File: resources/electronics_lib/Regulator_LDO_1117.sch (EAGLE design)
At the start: 3 parts

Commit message: Simplified some schematic blocks.
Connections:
- net 1_2V,#,+,O/1_8V,#,+,O/2_5V,#,+,O/2_85V,#,+,O/3_3V,#,+,O/5V,#,+,O renamed 3_3V,#,+,O
- net V_SUPPLY,#,+,I/V_BATT,#,+,I/2_5V,#,+,I/2_85V,#,+,I/3V,#,+,I/3_3V,#,+,I/3_6V,#,+,I/3_7V,#,+,I/4_5V,#,+,I/4_8V,#,+,I/5V,#,+,I/6V,#,+,I/7_2V,#,+,I/7_4V,#,+,I/7_5V,#,+,I/8_4V,#,+,I/9V,#,+,I/9_6V,#,+,I/10_5V,#,+,I/11_1V,#,+,I/12V,#,+,I renamed 5V,#,+,I
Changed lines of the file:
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@@
 </segment>
 </net>
-<net name="1_2V,#,+,O/1_8V,#,+,O/2_5V,#,+,O/2_85V,#,+,O/3_3V,#,+,O/5V,#,+,O" class="0">
+<net name="3_3V,#,+,O" class="0">
 <segment>
 <pinref part="C_BYP_OUT_1" gate="G$1" pin="1"/>
@@
 </segment>
 </net>
-<net name="V_SUPPLY,#,+,I/V_BATT,#,+,I/2_5V,#,+,I/2_85V,#,+,I/3V,#,+,I/3_3V,#,+,I/3_6V,#,+,I/3_7V,#,+,I/4_5V,#,+,I/4_8V,#,+,I/5V,#,+,I/6V,#,+,I/7_2V,#,+,I/7_4V,#,+,I/7_5V,#,+,I/8_4V,#,+,I/9V,#,+,I/9_6V,#,+,I/10_5V,#,+,I/11_1V,#,+,I/12V,#,+,I" class="0">
+<net name="5V,#,+,I" class="0">
 <segment>
 <pinref part="C_BYP_IN_1" gate="G$1" pin="1"/>

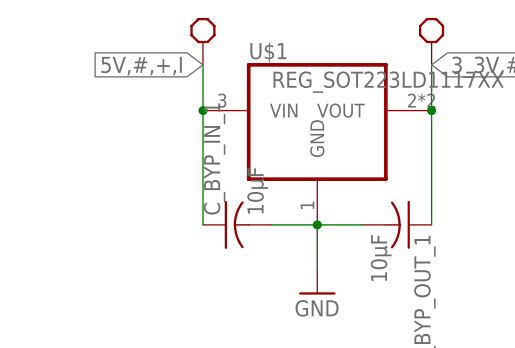
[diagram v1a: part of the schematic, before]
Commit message: Updated voltage setting in Regulator.
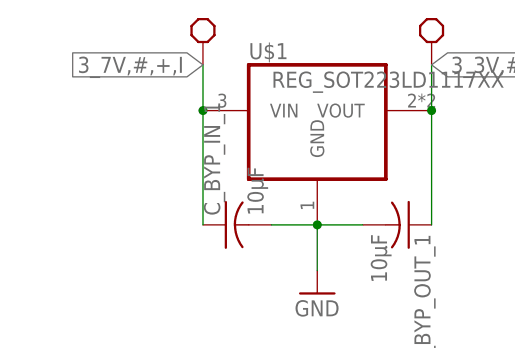
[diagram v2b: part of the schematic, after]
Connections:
- net 5V,#,+,I renamed 3_7V,#,+,I
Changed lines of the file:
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@@
 </segment>
 </net>
-<net name="5V,#,+,I" class="0">
+<net name="3_7V,#,+,I" class="0">
 <segment>
 <pinref part="C_BYP_IN_1" gate="G$1" pin="1"/>
